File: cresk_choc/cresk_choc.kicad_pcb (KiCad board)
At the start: 2 copper layers, 102 x 73 mm, 21 parts, among them J1 TRRS, J2 BATTERY, SW1 SW_Push, SW10 SW_Push, SW11 SW_Push, SW12 SW_Push, SW13 SW_Push, SW14 SW_Push, SW15 SW_Push, SW16 SW_Push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

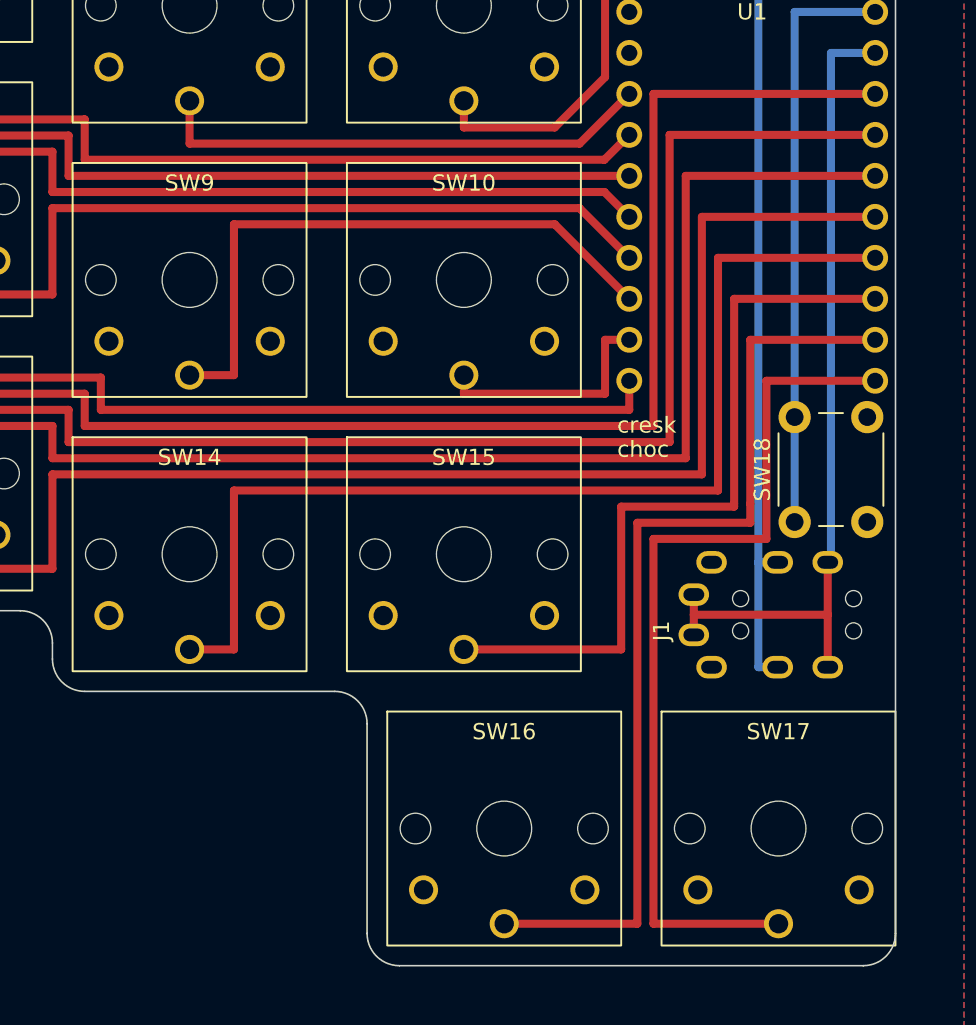
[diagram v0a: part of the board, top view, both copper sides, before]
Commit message: cresk_choc: update sw16 sw17 tracks
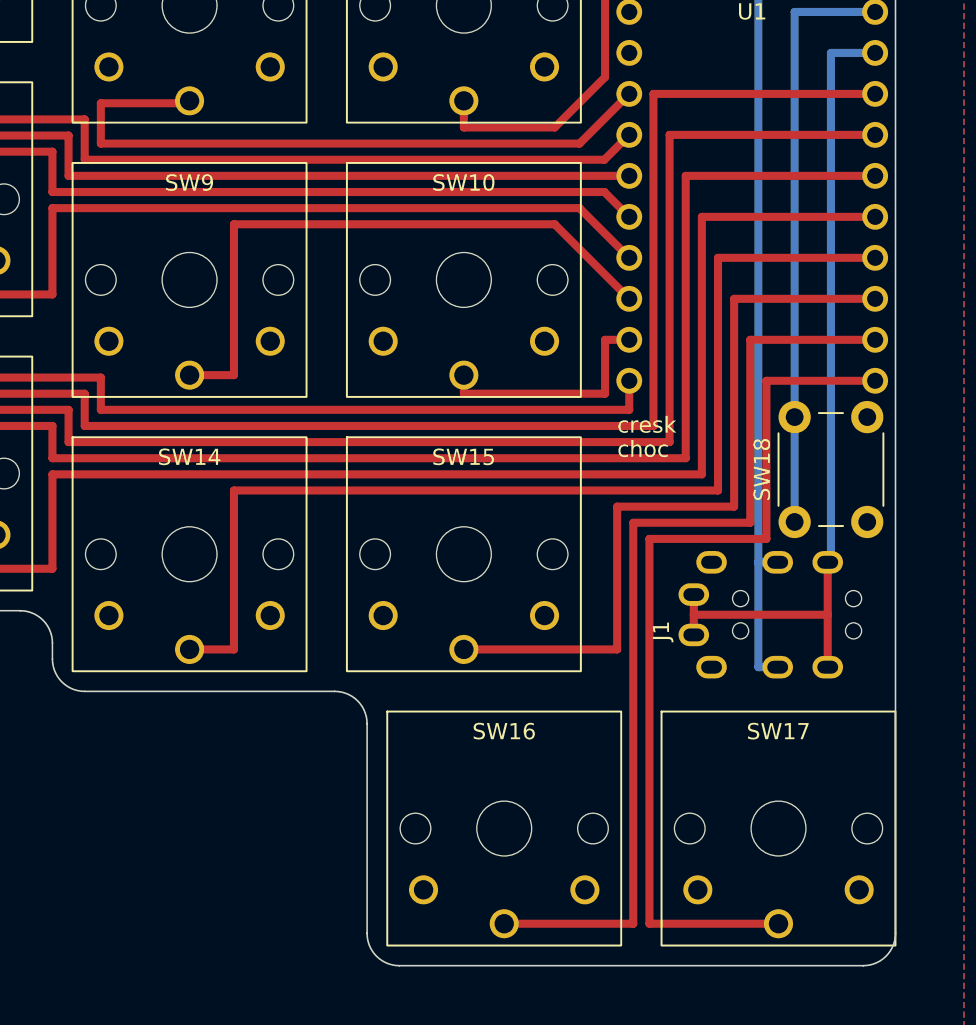
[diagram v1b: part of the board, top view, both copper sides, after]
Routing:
- net sw4: track 31.2 -> 42.0 mm
- net sw17: track 55.1 -> 55.6 mm
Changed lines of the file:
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@@
     )
     (pad_to_mask_clearance 0)
-    (grid_origin 119 55)
+    (grid_origin 129.25 65.55)
     (pcbplotparams
       (layerselection 0x00010fc_ffffffff)
@@
   (segment (start 95.5 62.05) (end 95.5 64.55) (width 0.5) (layer "F.Cu") (net 3))
   (segment (start 127.71 64.55) (end 129.25 63.01) (width 0.5) (layer "F.Cu") (net 3))
+  (segment (start 96.5 61.05) (end 102 61.05) (width 0.5) (layer "F.Cu") (net 4))
+  (segment (start 96.5 63.55) (end 96.5 61.05) (width 0.5) (layer "F.Cu") (net 4))
   (segment (start 129.25 60.47) (end 126.17 63.55) (width 0.5) (layer "F.Cu") (net 4))
-  (segment (start 102 63.55) (end 102 60.9) (width 0.5) (layer "F.Cu") (net 4))
-  (segment (start 126.17 63.55) (end 102 63.55) (width 0.5) (layer "F.Cu") (net 4))
+  (segment (start 126.17 63.55) (end 96.5 63.55) (width 0.5) (layer "F.Cu") (net 4))
   (segment (start 124.63 62.55) (end 119 62.55) (width 0.5) (layer "F.Cu") (net 5))
   (segment (start 127.75 50.31) (end 127.75 59.43) (width 0.5) (layer "F.Cu") (net 5))
@@
   (segment (start 102 94.9) (end 104.75 94.9) (width 0.5) (layer "F.Cu") (net 15))
   (segment (start 104.75 94.9) (end 104.75 85.05) (width 0.5) (layer "F.Cu") (net 15))
-  (segment (start 135.75 73.17) (end 135.75 85.87) (width 0.5) (layer "F.Cu") (net 16))
-  (segment (start 119 94.9) (end 128.75 94.9) (width 0.5) (layer "F.Cu") (net 16))
-  (segment (start 135.75 85.87) (end 135.75 86.05) (width 0.5) (layer "F.Cu") (net 16))
+  (segment (start 135.75 86.05) (end 128.5 86.05) (width 0.5) (layer "F.Cu") (net 16))
+  (segment (start 128.5 94.9) (end 119 94.9) (width 0.5) (layer "F.Cu") (net 16))
   (segment (start 144.49 73.17) (end 135.75 73.17) (width 0.5) (layer "F.Cu") (net 16))
-  (segment (start 128.75 94.9) (end 128.75 86.05) (width 0.5) (layer "F.Cu") (net 16))
-  (segment (start 135.75 86.05) (end 128.75 86.05) (width 0.5) (layer "F.Cu") (net 16))
-  (segment (start 121.5 111.9) (end 129.75 111.9) (width 0.5) (layer "F.Cu") (net 17))
-  (segment (start 129.75 111.9) (end 129.75 87.05) (width 0.5) (layer "F.Cu") (net 17))
-  (segment (start 136.75 87.05) (end 129.75 87.05) (width 0.5) (layer "F.Cu") (net 17))
-  (segment (start 136.75 85.87) (end 136.75 75.71) (width 0.5) (layer "F.Cu") (net 17))
-  (segment (start 136.75 75.71) (end 144.49 75.71) (width 0.5) (layer "F.Cu") (net 17))
-  (segment (start 136.75 85.87) (end 136.75 87.05) (width 0.5) (layer "F.Cu") (net 17))
-  (segment (start 130.75 88.05) (end 137.75 88.05) (width 0.5) (layer "F.Cu") (net 18))
-  (segment (start 137.75 88.05) (end 137.75 78.25) (width 0.5) (layer "F.Cu") (net 18))
-  (segment (start 130.75 111.9) (end 130.75 88.05) (width 0.5) (layer "F.Cu") (net 18))
-  (segment (start 138.5 111.9) (end 130.75 111.9) (width 0.5) (layer "F.Cu") (net 18))
-  (segment (start 137.75 78.25) (end 144.49 78.25) (width 0.5) (layer "F.Cu") (net 18))
+  (segment (start 128.5 86.05) (end 128.5 94.9) (width 0.5) (layer "F.Cu") (net 16))
+  (segment (start 135.75 73.17) (end 135.75 86.05) (width 0.5) (layer "F.Cu") (net 16))
+  (segment (start 136.75 87.05) (end 129.5 87.05) (width 0.5) (layer "F.Cu") (net 17))
+  (segment (start 129.5 87.05) (end 129.5 111.9) (width 0.5) (layer "F.Cu") (net 17))
+  (segment (start 144.49 75.71) (end 136.75 75.71) (width 0.5) (layer "F.Cu") (net 17))
+  (segment (start 136.75 75.71) (end 136.75 87.05) (width 0.5) (layer "F.Cu") (net 17))
+  (segment (start 121.5 111.9) (end 129.5 111.9) (width 0.5) (layer "F.Cu") (net 17))
+  (segment (start 130.5 111.9) (end 138.5 111.9) (width 0.5) (layer "F.Cu") (net 18))
+  (segment (start 144.49 78.25) (end 137.75 78.25) (width 0.5) (layer "F.Cu") (net 18))
+  (segment (start 137.75 88.05) (end 130.5 88.05) (width 0.5) (layer "F.Cu") (net 18))
+  (segment (start 137.75 78.25) (end 137.75 88.05) (width 0.5) (layer "F.Cu") (net 18))
+  (segment (start 130.5 88.05) (end 130.5 111.9) (width 0.5) (layer "F.Cu") (net 18))
   (segment (start 139.5 55.39) (end 144.49 55.39) (width 0.5) (layer "B.Cu") (net 19))
   (segment (start 139.5 80.5) (end 139.5 87) (width 0.5) (layer "B.Cu") (net 19))
